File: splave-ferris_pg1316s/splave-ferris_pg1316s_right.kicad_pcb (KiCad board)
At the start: 2 copper layers, 117.9 x 85.9 mm, 37 parts

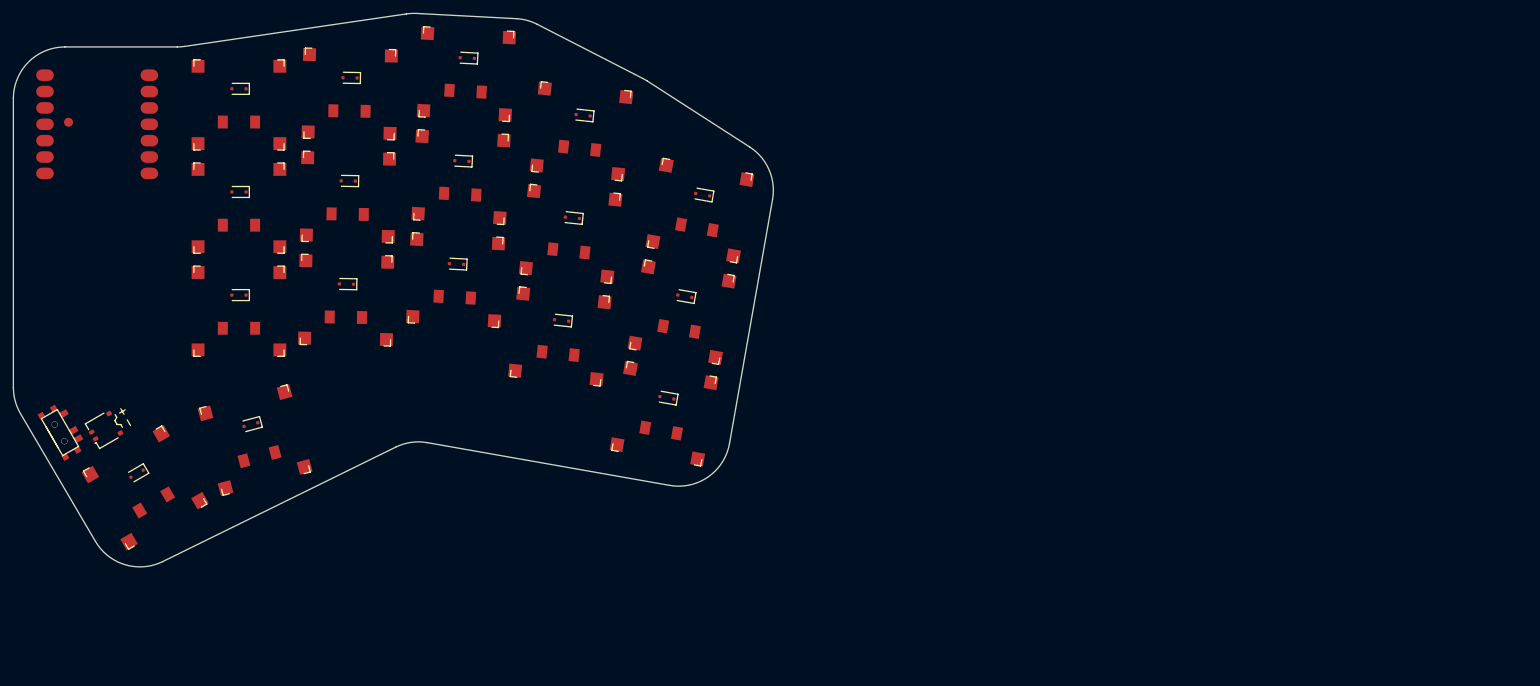
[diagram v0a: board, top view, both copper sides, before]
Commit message: Complete routing for PG1316S variant, create production files.
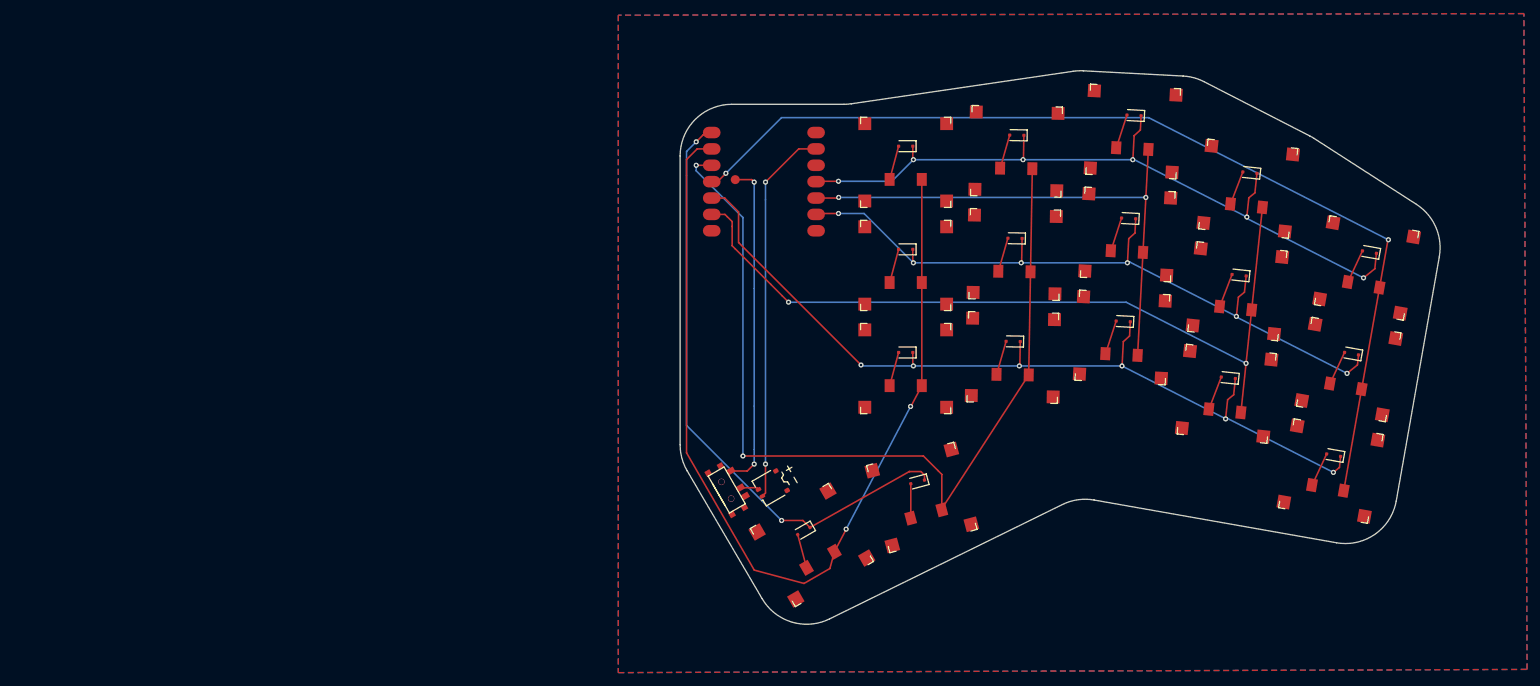
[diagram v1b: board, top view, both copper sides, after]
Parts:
- D1, D10, D11, D12, D13, D14, D15, D16, D17, D2, D3, D4, D5, D6, D7, D8, D9: footprint diode_smd_sod323f -> D_SOD-323F
- moved S15 103.8 mm to (269.6, 96.8)
- moved S6 103.8 mm to (322.7, 100.9)
- moved D5 103.8 mm to (321.3, 114.3)
- moved D4 103.8 mm to (319.6, 130.3)
- moved D13 103.8 mm to (269.6, 126.3)
- moved D6 103.8 mm to (323.0, 98.4)
- moved D15 103.8 mm to (269.6, 94.3)
- moved MCU1 103.8 mm to (247.6, 99.8)
- moved S2 103.8 mm to (338.3, 129.0)
- moved D16 103.8 mm to (271.4, 146.4)
- moved S1 103.8 mm to (335.5, 144.7)
- moved D17 103.8 mm to (253.8, 154.0)
- moved D10 103.8 mm to (286.3, 124.6)
- moved D12 103.8 mm to (286.8, 92.6)
- moved S12 103.8 mm to (286.8, 95.1)
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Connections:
- T1 pad 2: BATCON -> BAT_P
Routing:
- net D3: track 0.00 -> 152.7 mm, vias 0 -> 2
- net D1: track 0.00 -> 148.0 mm, vias 0 -> 2
- net D2: track 0.00 -> 145.5 mm, vias 0 -> 2
- net D4: track 0.00 -> 136.5 mm, vias 0 -> 6
- net D5: track 0.00 -> 124.5 mm, vias 0 -> 2
- net D10: track 0.00 -> 116.5 mm, vias 0 -> 6
- net D8: track 0.00 -> 113.9 mm, vias 0 -> 6
- net D0: track 0.00 -> 94.9 mm, vias 0 -> 2
- net D9: track 0.00 -> 83.7 mm, vias 0 -> 2
- net GND: track 0.00 -> 58.4 mm, vias 0 -> 2
- net BAT: track 0.00 -> 50.9 mm, vias 0 -> 2
- net mirror_middle_home: track 0.00 -> 5.34 mm
- net mirror_index_bottom: track 0.00 -> 5.34 mm
- net mirror_middle_bottom: track 0.00 -> 5.34 mm
- net mirror_far_fan: track 0.00 -> 5.34 mm
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- added copper zone on B.Cu, net (none)
- added copper zone on F.Cu, net (none)
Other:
- net class Default removed
